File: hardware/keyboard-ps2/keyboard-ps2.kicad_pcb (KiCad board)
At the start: 2 copper layers, 93.3 x 68.6 mm, 35 parts, among them J1 DB25F, J2 PS2_CONN, U1 74HC595, U10 74HC595, U11 74HC595, U12 ATMEGA328P, U2 74HC595, U3 74HC595, U4 74HC595, U5 74HC595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

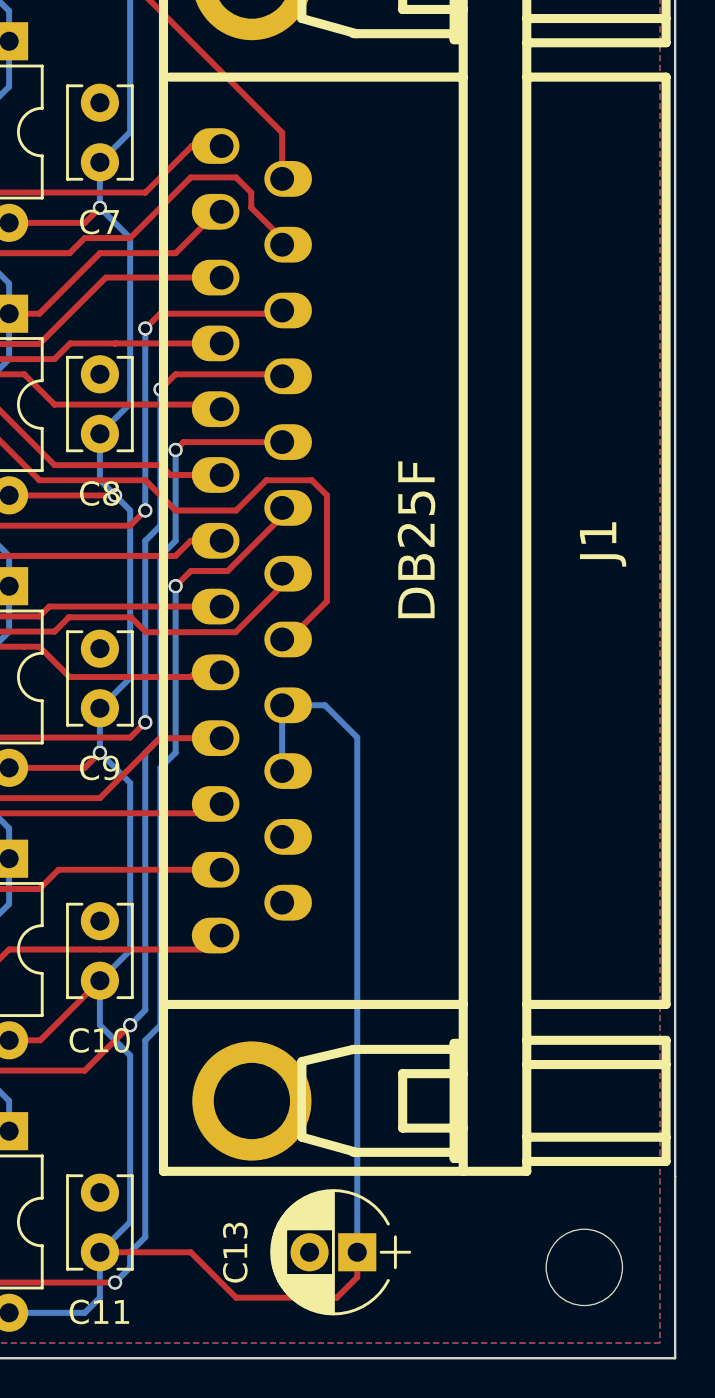
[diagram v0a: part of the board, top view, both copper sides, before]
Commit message: Add pins for optional pin header in DB25 footprints
We might want to use an internal connection to a pin header of 100millis instead of the DB25 connector. So we have included additional pins to sold such pin header instead of DB25 header.
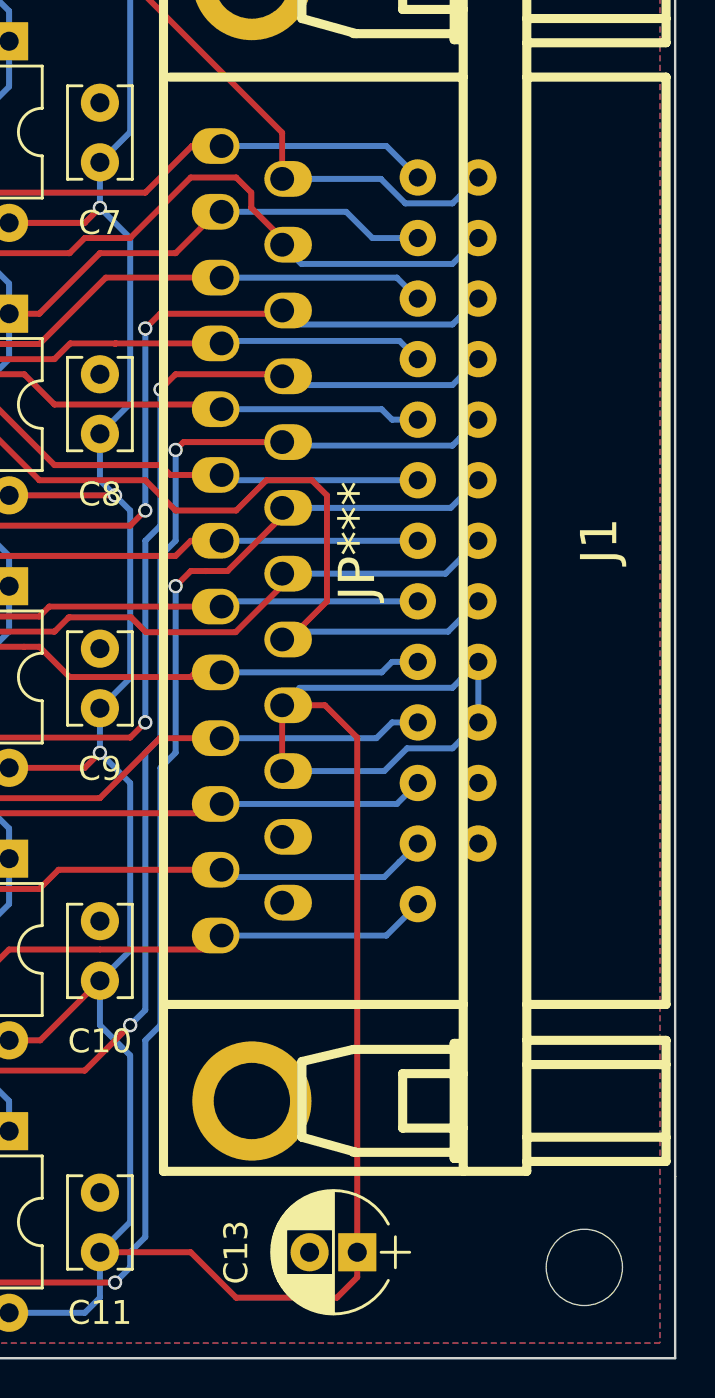
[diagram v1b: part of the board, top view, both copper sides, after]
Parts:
- J1: value DB25F -> JP***
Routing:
- net ~: track 426.5 -> 447.1 mm
- net /~RSL5: track 24.2 -> 33.3 mm
- net /~RSL6: track 22.6 -> 31.6 mm
- net /~RSL3: track 47.8 -> 56.7 mm
- net /~RSL7: track 27.8 -> 36.7 mm
- net /~RESET: track 81.0 -> 89.9 mm
- net /~RSL8: track 33.8 -> 42.6 mm
- net /~CAPSL: track 75.2 -> 84.0 mm
- net /~RSL4: track 47.8 -> 56.6 mm
- net /KBCOL0: track 152.2 -> 161.0 mm
- net /~RSL9: track 43.5 -> 52.3 mm
- net /~RSL10: track 48.9 -> 57.6 mm
- net /KBCOL1: track 150.9 -> 159.5 mm
- net /~RSL2: track 57.6 -> 66.2 mm
- net /KBCOL2: track 152.6 -> 161.2 mm
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
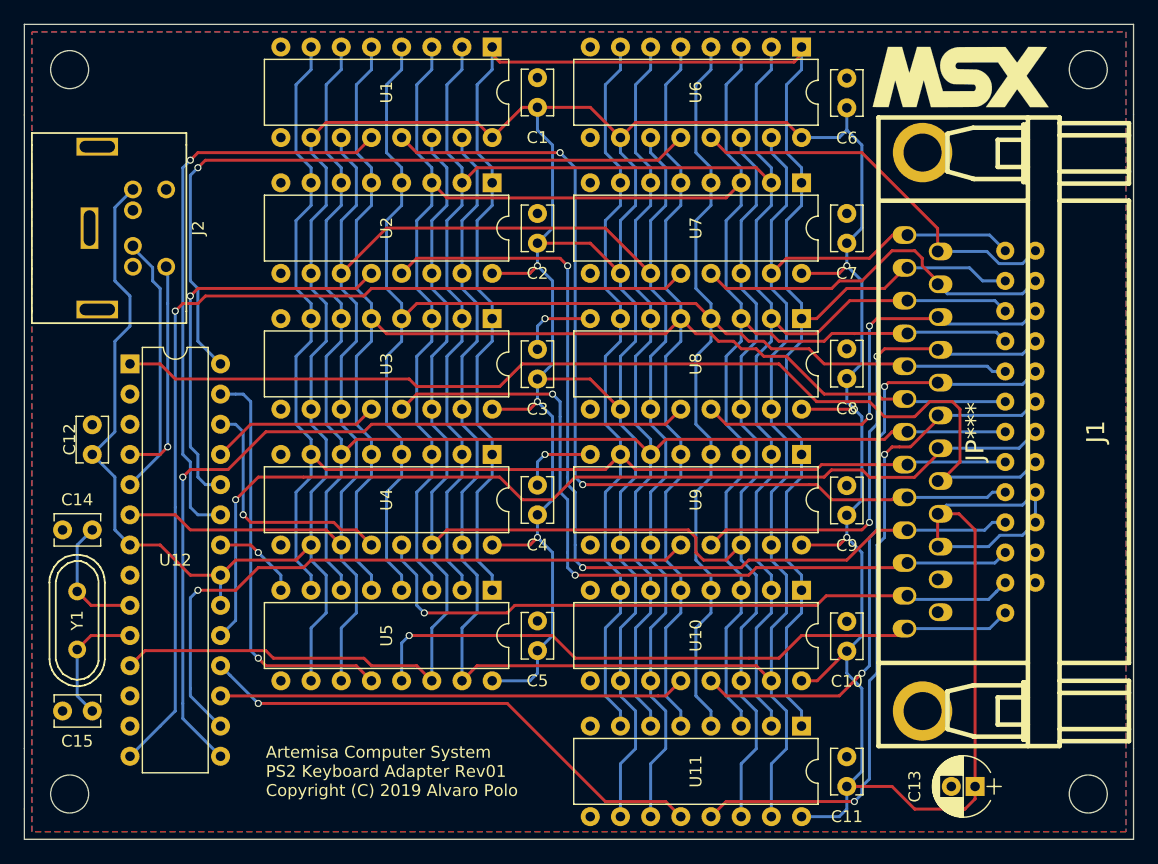
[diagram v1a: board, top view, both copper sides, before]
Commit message: Add KANALOCK signals to keyboard connectors
Still not used from the motherboard (wired to 5v).
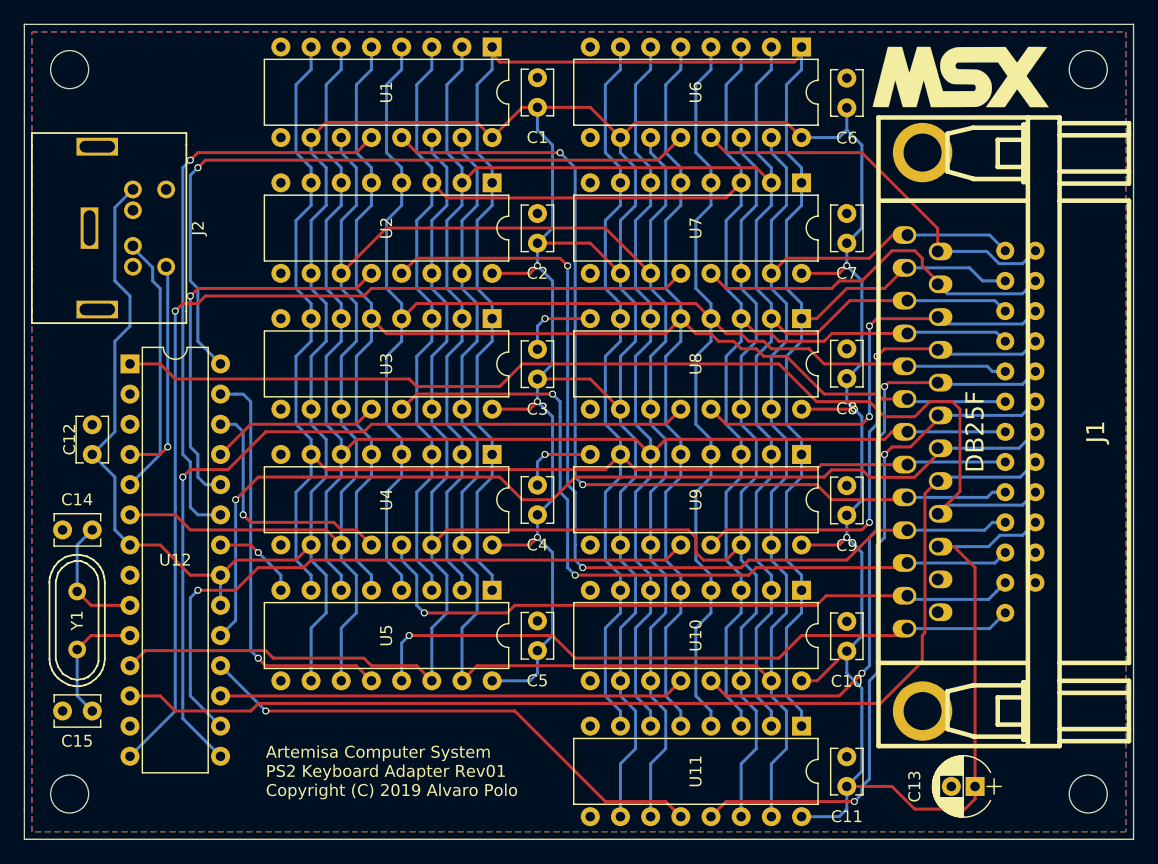
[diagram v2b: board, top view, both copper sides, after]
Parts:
- J1: value JP*** -> DB25F
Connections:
- net /~CAPSL renamed /~CAPSLOCK
- J1 pad 21: /~RESET -> /~KANALOCK
- J1 pad 22: ~ -> /~RESET
- U12 pad 12: Net-(U12-Pad12) -> /~KANALOCK
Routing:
- net /~KANALOCK: track 0.00 -> 93.6 mm
- net ~: track 447.1 -> 429.8 mm
- net /~RESET: track 89.9 -> 92.6 mm

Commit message: Fix DB25 connector of keyboard PS2 PCB
So it stands out from the board.
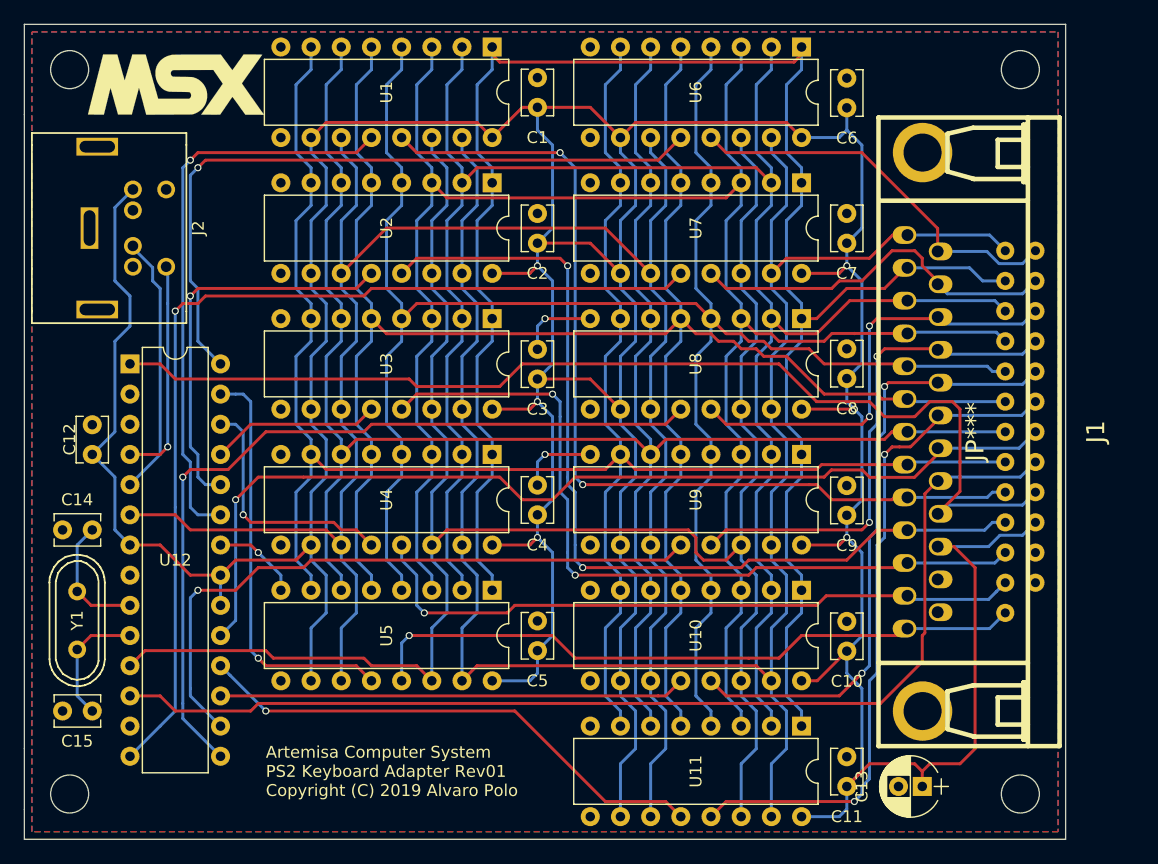
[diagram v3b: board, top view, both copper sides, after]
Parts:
- J1: value DB25F -> JP***
- moved G*** 66.0 mm to (108.0, 69.8)
- moved REF** 5.72 mm to (179.1, 68.6)
- moved REF** 5.72 mm to (179.1, 129.5)
- moved C13 4.44 mm to (170.8, 128.9)
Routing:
- net ~: track 429.8 -> 427.6 mm
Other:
- board size 93.3 x 68.6 mm -> 87.6 x 68.6 mm
